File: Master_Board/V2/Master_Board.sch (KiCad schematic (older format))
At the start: 3 parts, among them J101 649022227222

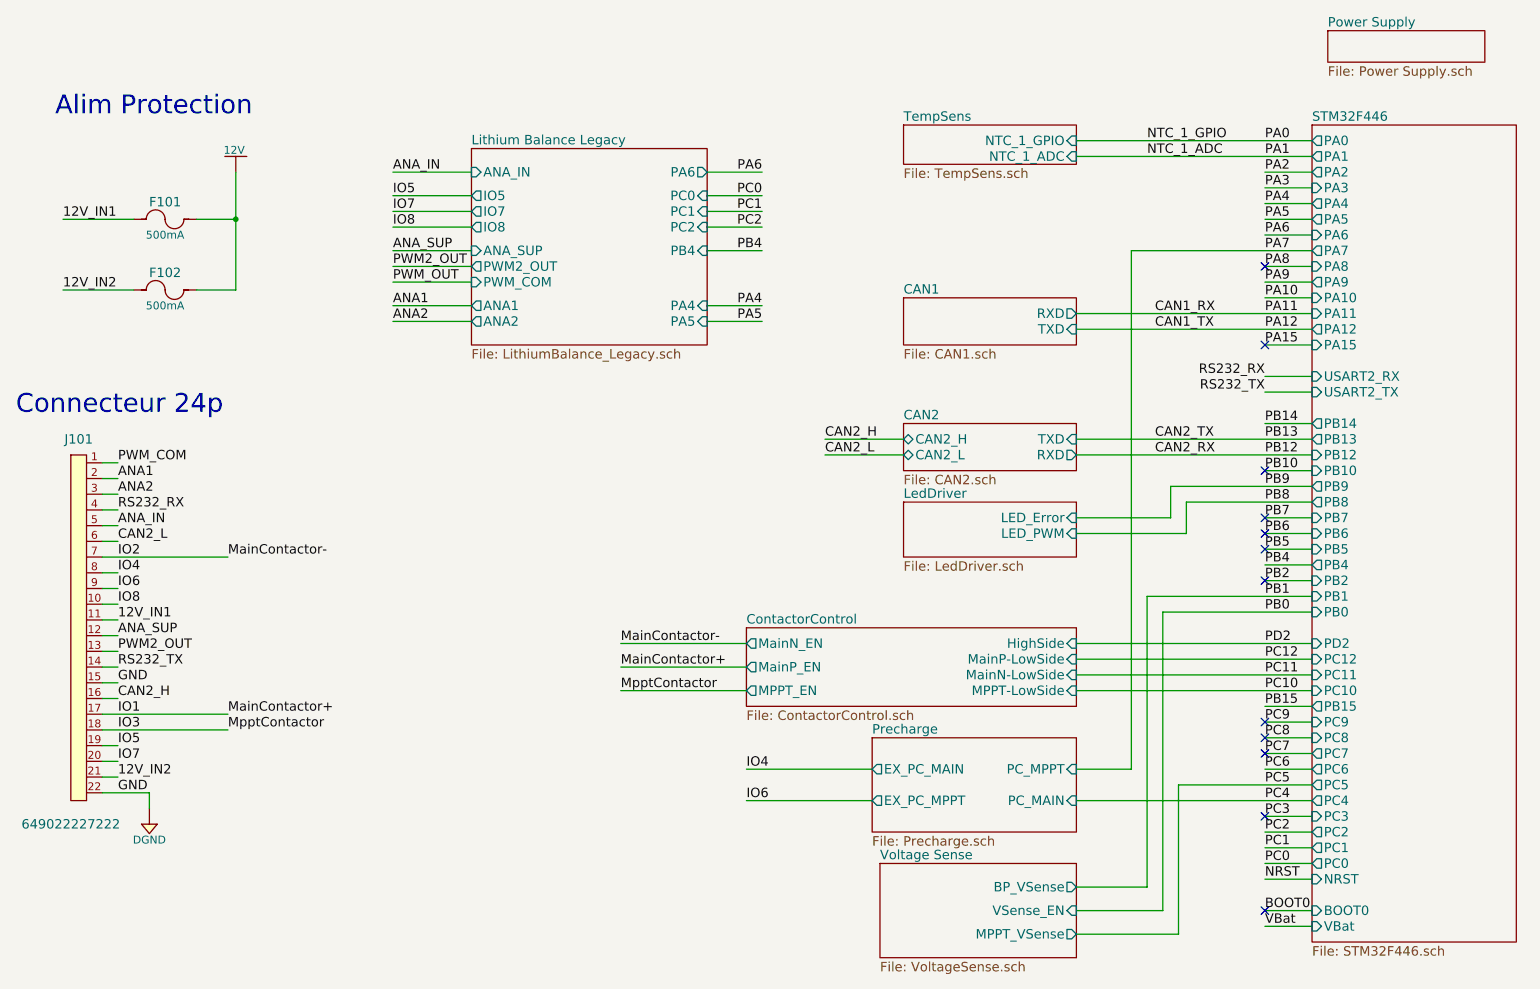
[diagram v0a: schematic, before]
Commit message: Place part in PCB
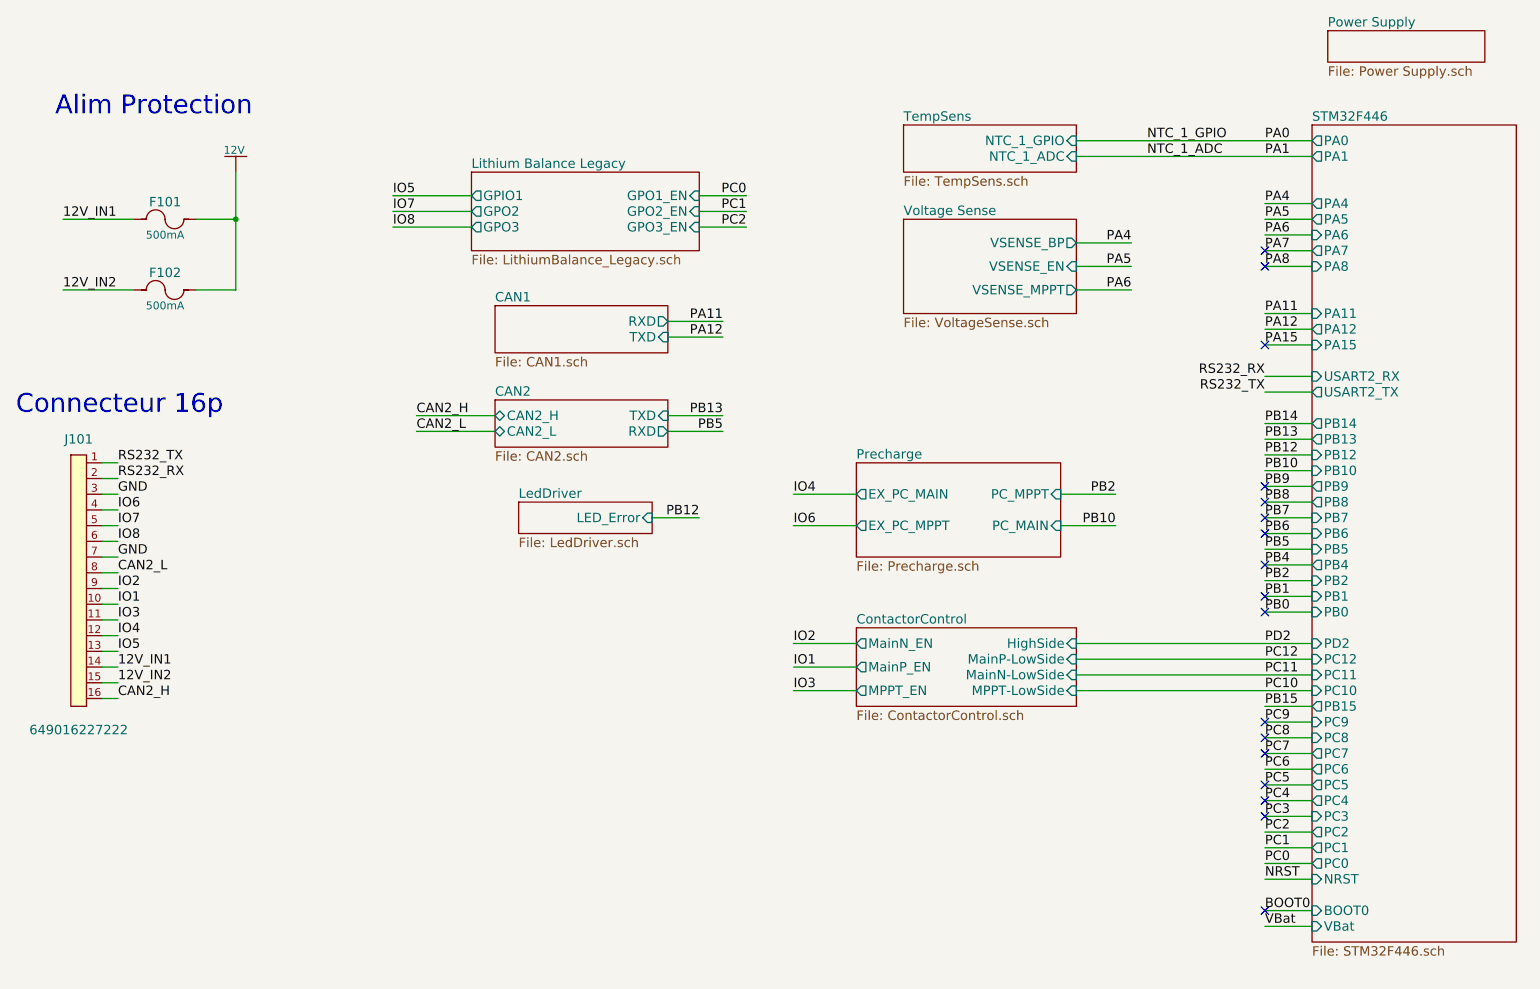
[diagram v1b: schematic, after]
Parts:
- removed J101: 649022227222, Connectors:649022227222, symbol 649022227222
- added J101: 649016227222, Connectors:649016227222, symbol 649016227222
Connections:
- net 12V_IN1: now also J101.14
- net 12V_IN2: now also J101.15
- net CAN2_H: now also J101.16
- net CAN2_L: now also J101.8
- net IO1: now also J101.10
- net IO2: now also J101.9
- net IO3: now also J101.11
- net IO4: now also J101.12
- net IO5: now also J101.13
- net IO6: now also J101.4
- net IO7: now also J101.5
- net IO8: now also J101.6
- net RS232_RX: now also J101.2
- net RS232_TX: now also J101.1
- new net GND: J101.3, J101.7
- no-connect marks 12 -> 17
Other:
- note added: "Connecteur 16p"
- note removed: "Connecteur 24p"

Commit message: Route small traces
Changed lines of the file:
@@
 F41 "PA7" O L 9000 2100 60
 F42 "NRST" I L 9000 6100 60
-F43 "USART2_RX" I L 9000 2900 60
-F44 "USART2_TX" O L 9000 3000 60
+F43 "USART1_RX" I L 9000 2900 60
+F44 "USART1_TX" O L 9000 3000 60
 $EndSheet
 $Sheet
